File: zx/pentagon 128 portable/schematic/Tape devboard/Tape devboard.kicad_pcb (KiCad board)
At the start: 2 copper layers, 26 x 31 mm, 15 parts, among them IC13 74HCT3G14DP,125, J1 Conn_01x02, J2 Conn_01x09, J3 Conn_02x02_Odd_Even, U10 74LS244

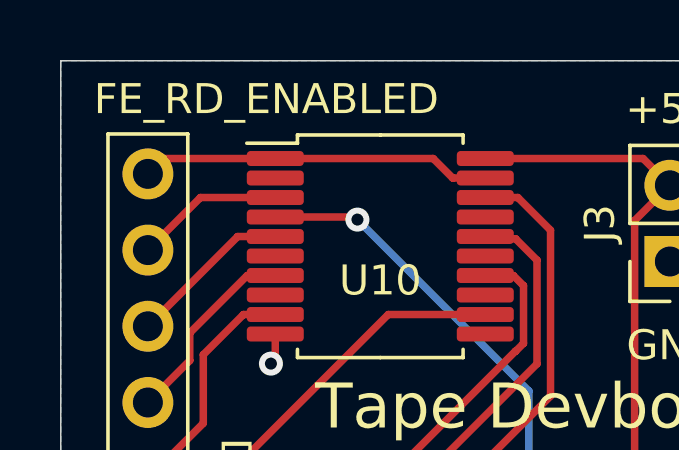
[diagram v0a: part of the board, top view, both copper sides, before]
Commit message: added z80 pdip. updated all boards
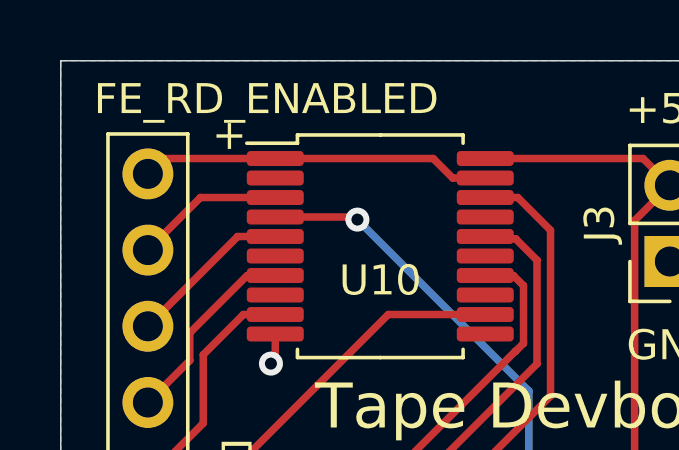
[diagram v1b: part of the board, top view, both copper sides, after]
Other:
- board text added: "+"
- board text added: "JLCJLCJLCJLC"
